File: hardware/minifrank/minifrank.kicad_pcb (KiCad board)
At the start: 4 copper layers, 85.6 x 54 mm, 136 parts, among them J1 PWR, J10 VGA, J11 PJ-320D, J12 104031-0811, J2 UART, J3 DEBUG, J4 SS-52100-004, J5 USB4215-03-A, J6 MDC-036, J7 PJ-320D, J8 DC3RX19JA2, J9 GP2, U1 TS3USB221RSER, U10 ESP-01v090, U11 TDA1387T, U12 LM358, U2 USBLC6-2SC6, U3 MW7211A, U4 AMS1117-3.3, U5 TXS0104ERGYR, U6 ESP-PSRAM32, U7 W25Q128JVS, U8 CD4069UBM, U9 RP2350, Y1 ASE-12MHz

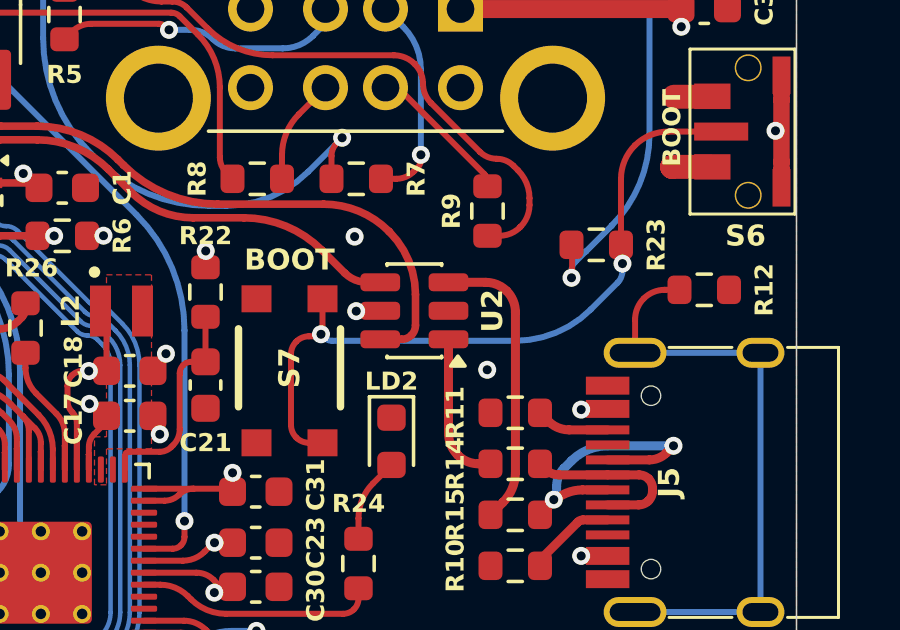
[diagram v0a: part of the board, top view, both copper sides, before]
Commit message: MiniFRANK: localize libs, recolor connectors, split audio jacks
- Split J7 (TapeIn) and J11 (AudioOut) into per-instance footprints
  and 3D models with light red and green plastic
- Unify connector metal shells to neutral 0.65 gray (USB, USB-C, SD,
  PS/2, switches, DB9, VGA, HDMI)
- Color VGA plastic body blue
- Replace HDMI IGES with project-local STEP and align footprint
- Move all 3D models and footprints to project-local 3d/ and libs/
- Merge cached schematic symbols into FRANK.kicad_sym; rewrite all
  schematic instances to use FRANK: lib_id; trim sym-lib-table
- Run kicad-cli sym/sch upgrade so cached symbols match library
- Remove unused footprints, symbols, and 3D files
- Regenerate minifrank-iso.png
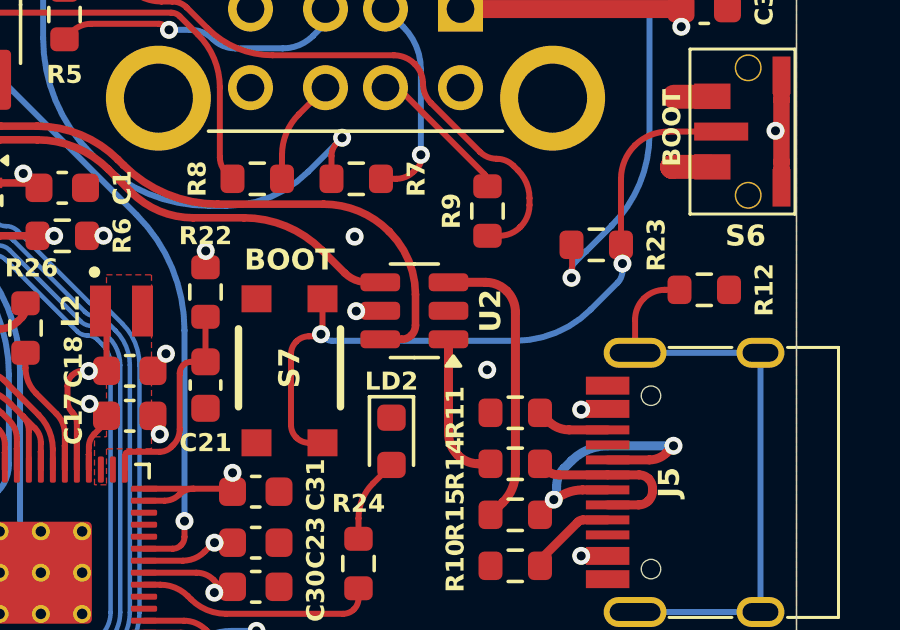
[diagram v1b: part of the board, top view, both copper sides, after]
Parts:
- J11: footprint FRANK:Jack (3.5mm, PJ-320D) -> FRANK:Jack (3.5mm, PJ-320D, AudioOut)
- J7: footprint FRANK:Jack (3.5mm, PJ-320D) -> FRANK:Jack (3.5mm, PJ-320D, TapeIn)
- U2: footprint Package_TO_SOT_SMD:SOT-23-6 -> FRANK:SOT-23-6

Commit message: fix: correct PSRAM part to ESP-PSRAM64H and clean up doc inaccuracies
Hardware:
- Rename ESP-PSRAM32 to ESP-PSRAM64H across MicroFRANK and MiniFRANK
  symbol libraries, schematics, PCB value fields and the SO-8 footprint
  default. Update datasheet URL to Espressif's combined ESP-PSRAM64 /
  ESP-PSRAM64H sheet.

Docs:
- Replace "SD card with firmware" wording everywhere with the correct
  "SD card with ROMs / disk images" plus an explicit BOOTSEL -> .uf2
  flashing step. RP2040 and RP2350 are not flashable from SD; the SD
  card holds runtime content read by the firmware.
- MicroFRANK: drop bogus TXS0104ERGYR from BOM and soldering steps;
  the part is not on this board (no PS/2, no gamepad, no 5 V signals).
- FRANK PGA: split the misleading "1 vs 2 audio multiplexer" comparison
  into separate audio-mux and USB-host-mux rows; FRANK PGA uses two
  74HC4052D, one for audio routing and one as the USB D+/D- multiplexer.
  Remove the stale TS3USB221 mention from the soldering steps.
- README and all four board guides (EN + RU): PSRAM type now reads
  ESP-PSRAM64H consistently.
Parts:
- U6: value ESP-PSRAM32 -> ESP-PSRAM64H
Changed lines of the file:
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@@
 			)
 		)
-		(property "Value" "ESP-PSRAM32"
+		(property "Value" "ESP-PSRAM64H"
 			(at 0 3.4 0)
 			(layer "F.Fab")
@@
 			)
 		)
-		(property "Datasheet" "https://www.espressif.com/sites/default/files/documentation/esp-psram32_datasheet_en.pdf"
+		(property "Datasheet" "https://www.espressif.com/sites/default/files/documentation/esp-psram64_esp-psram64h_datasheet_en.pdf"
 			(at 0 0 0)
 			(layer "F.Fab")

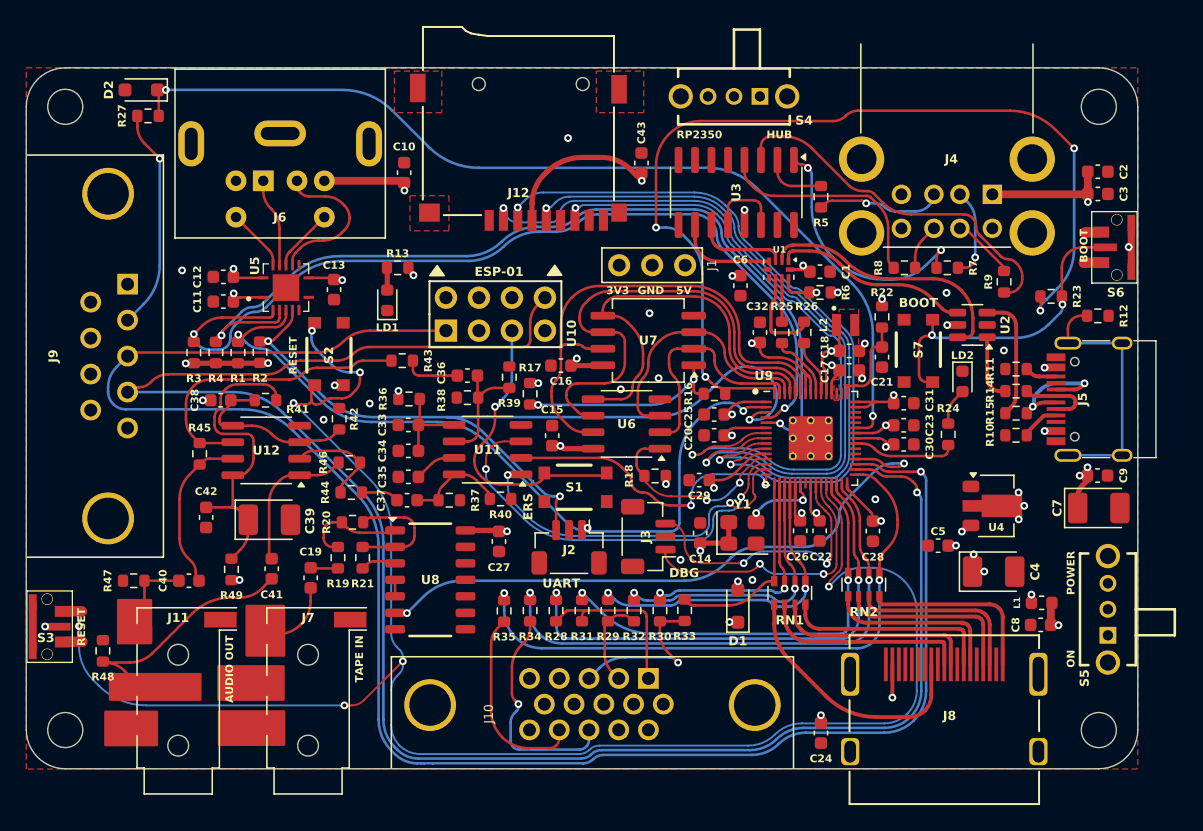
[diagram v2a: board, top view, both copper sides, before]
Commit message: docs: standardize naming (assembly.pdf, bom.html, schematics.pdf)
Latest versions:
- frank: 2.09
- frank_pga: 1.03
- microfrank: 1.02
- minifrank: 1.07
- nyx: 2.03
- xt8086: 1.04
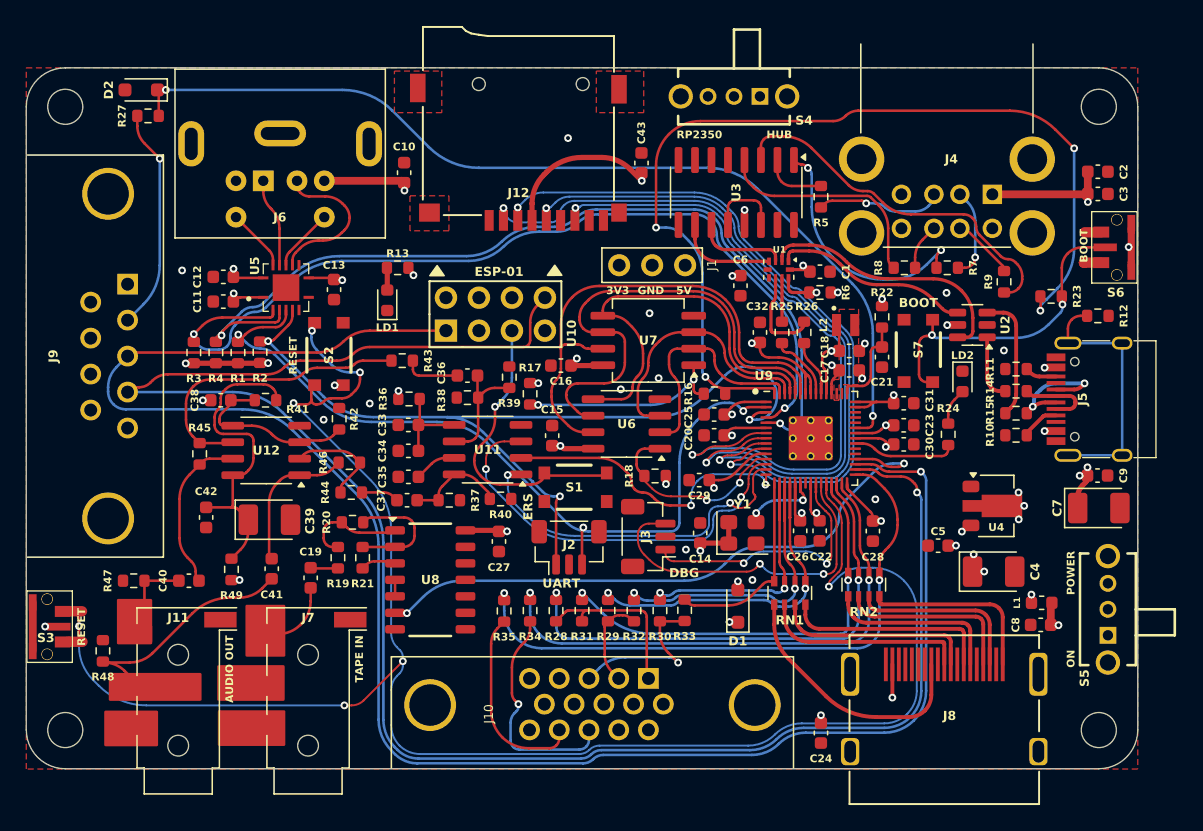
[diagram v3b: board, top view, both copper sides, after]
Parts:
- turned J2 to 0 degrees
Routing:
- net /RP2350A/SWD: track 21.7 -> 26.9 mm
- net /GPIO0: track 59.2 -> 62.1 mm
- net /GPIO1: track 65.9 -> 68.5 mm
- net /RP2350A/SWCLK: track 22.0 -> 21.2 mm

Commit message: MiniFRANK: new board version
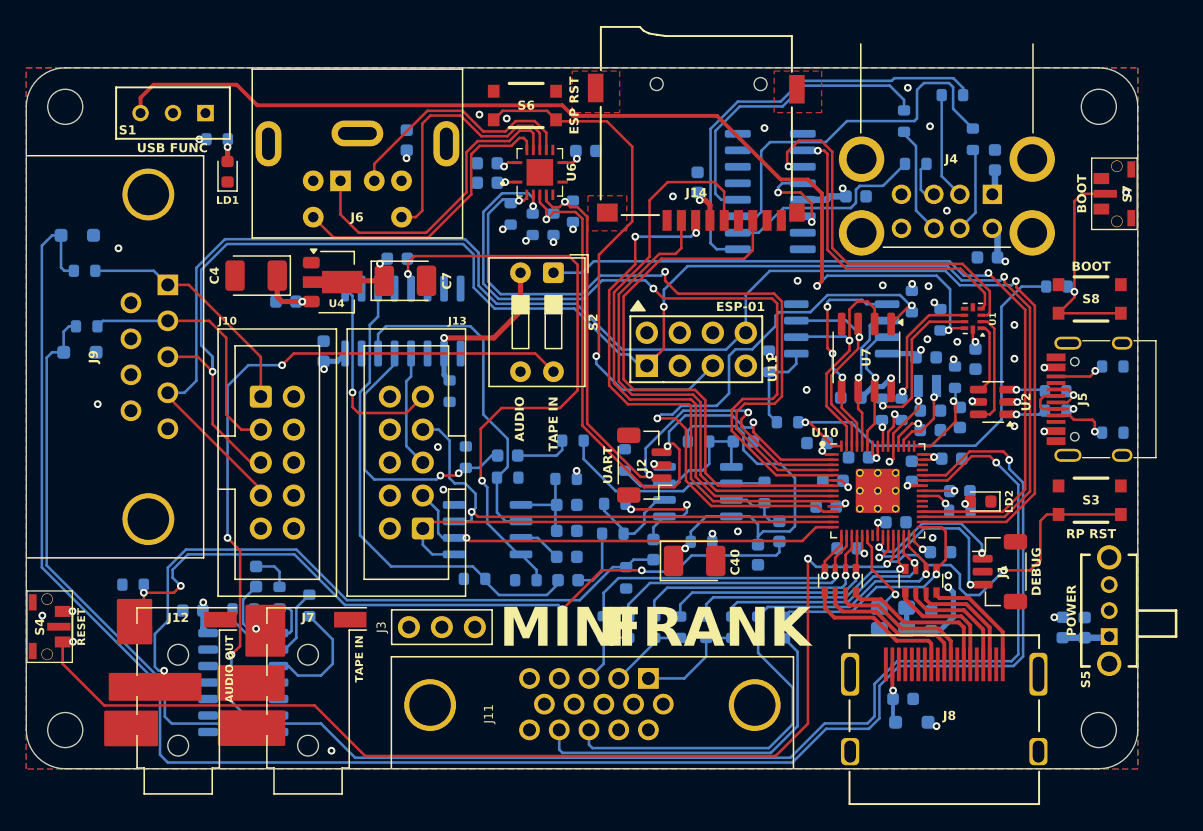
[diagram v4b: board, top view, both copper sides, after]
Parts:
- removed the R12 at (213.2, 82.9)
- removed the S4 at (187.2, 66.0)
- added C10: 100n, FRANK:C_0603_1608Metric, B.Cu at (153.6, 85.6)
- added D2: 3V3, FRANK:D_SOD-323, B.Cu at (134.6, 76.7)
- added J10: Conn_02x05_Top_Bottom, FRANK:IDC-Header_2x05_P2.54mm_Vertical, F.Cu at (148.8, 89.1)
- added J13: Ext_Sound, FRANK:IDC-Header_2x05_P2.54mm_Vertical, F.Cu at (161.2, 99.3)
- added R15: 10K, FRANK:R_0603_1608Metric, B.Cu at (163.3, 88.7)
- added R27: 1K, FRANK:R_0603_1608Metric, B.Cu at (135.2, 79.4)
- added S1: SS12D00, FRANK:Switch_Slide_SS12D00, F.Cu at (144.5, 67.3)
- added S2: SW_DIP_x02, FRANK:SW_DIP_SPSTx02_Slide_9.78x7.26mm_W7.62mm_P2.54mm, F.Cu at (171.3, 79.6)
- added U5: 74HC4052D, FRANK:SOP-16_P1.27mm, B.Cu at (159.7, 83.3)
- C1, C2, C3, C5, C6, C8, C9, L1, L2, R10, R11, R16, R17, R18, R19, R20, R21, R22, R23, R24, R25, R26, R5, R6, R7, R8, R9, U3, Y1: moved to B.Cu
- C11: renamed from C10; moved to B.Cu
- C12: renamed from C11; moved to B.Cu
- C13: renamed from C12; moved to B.Cu
- C14: renamed from C13; moved to B.Cu
- C15: renamed from C14; moved to B.Cu
- C16: renamed from C15; moved to B.Cu
- C17: renamed from C16; moved to B.Cu
- C18: renamed from C17; moved to B.Cu
- C19: renamed from C18; moved to B.Cu
- C20: renamed from C19; moved to B.Cu
- C21: renamed from C20; moved to B.Cu
- C22: renamed from C21; moved to B.Cu
- C23: renamed from C22; moved to B.Cu
- C24: renamed from C23; moved to B.Cu
- C25: renamed from C24; moved to B.Cu
- C26: renamed from C25; moved to B.Cu
- C27: renamed from C26; moved to B.Cu
- C28: renamed from C27; moved to B.Cu
- C29: renamed from C28; moved to B.Cu
- C30: renamed from C29; moved to B.Cu
- C31: renamed from C30; moved to B.Cu
- C32: renamed from C31; moved to B.Cu
- C33: renamed from C32; moved to B.Cu
- C34: renamed from C33; moved to B.Cu
- C35: renamed from C34; moved to B.Cu
- C36: renamed from C35; moved to B.Cu
- C37: renamed from C36; moved to B.Cu
- C38: renamed from C37; moved to B.Cu
- C39: renamed from C38; moved to B.Cu
- C4, C7: footprint FRANK:Capacitor (3528, tantalum, polar) -> FRANK:CP_EIA-3528-12_Kemet-T
- C40: renamed from C39; footprint FRANK:Capacitor (3528, tantalum, polar) -> FRANK:CP_EIA-3528-12_Kemet-T
- C41: renamed from C40; moved to B.Cu
- C42: renamed from C41; moved to B.Cu
- C43: renamed from C42; moved to B.Cu
- C44: renamed from C43; moved to B.Cu
- D1: footprint FRANK:Diode (SOD-323) -> FRANK:D_SOD-323; moved to B.Cu
- D3: renamed from D2; footprint FRANK:Diode (SOD-323) -> FRANK:D_SOD-323; moved to B.Cu
- H1, H2, H3, H4: footprint FRANK:Mounting Hole (2.7mm) -> FRANK:MountingHole_2.7mm
- J11: renamed from J10; footprint FRANK:D-SUB (15 pin, female) -> FRANK:DSUB-15_Female
- J12: renamed from J11; footprint FRANK:Jack (3.5mm, PJ-320D, AudioOut) -> FRANK:AudioJack_3.5mm_PJ320D_AudioOut
- J14: renamed from J12; footprint FRANK:MicroSD (SMD, long) -> FRANK:MicroSD_SMD_Long
- J3: renamed from J1; footprint FRANK:Pin Header (1x03) -> FRANK:PinHeader_1x03_P2.54mm
- J4: footprint FRANK:USB Type A (stacked) -> FRANK:USB_A_Stacked
- J5: footprint FRANK:USB Type C -> FRANK:USB_C_Receptacle
- J6: footprint FRANK:MiniDIN (6 Pin, female) -> FRANK:MiniDIN_6pin_Female
- J7: footprint FRANK:Jack (3.5mm, PJ-320D, TapeIn) -> FRANK:AudioJack_3.5mm_PJ320D_TapeIn
- J8: footprint FRANK:HDMI (female) -> FRANK:HDMI_Female
- J9: footprint FRANK:D-SUB (9 pin, male, top mount) -> FRANK:DSUB-9_Male_TopMount
- R1: renamed from R3; moved to B.Cu
- R12: renamed from R13; moved to B.Cu
- R13: renamed from R14; moved to B.Cu
- R14: renamed from R15; moved to B.Cu
- R2: renamed from R4; moved to B.Cu
- R28: renamed from R27; moved to B.Cu
- R29: renamed from R28; moved to B.Cu
- R3: renamed from R1; moved to B.Cu
- R30: renamed from R29; moved to B.Cu
- R31: renamed from R30; moved to B.Cu
- R32: renamed from R31; moved to B.Cu
- R33: renamed from R32; moved to B.Cu
- R34: renamed from R33; moved to B.Cu
- R35: renamed from R34; moved to B.Cu
- R36: renamed from R35; moved to B.Cu
- R37: renamed from R36; moved to B.Cu
- R38: renamed from R37; moved to B.Cu
- R39: renamed from R38; moved to B.Cu
- R4: renamed from R2; moved to B.Cu
- R40: renamed from R39; moved to B.Cu
- R41: renamed from R40; moved to B.Cu
- R42: renamed from R41; moved to B.Cu
- R43: renamed from R42; moved to B.Cu
- R44: renamed from R43; moved to B.Cu
- R45: renamed from R44; moved to B.Cu
- R46: renamed from R45; moved to B.Cu
- R47: renamed from R46; moved to B.Cu
- R48: renamed from R47; moved to B.Cu
- R49: renamed from R48; moved to B.Cu
- R50: renamed from R49; moved to B.Cu
- RN1, RN2: footprint FRANK:Resistor Array (4x0603) -> FRANK:R_Array_4x0603
- U10: renamed from U9; footprint FRANK:QFN 60 (RP2350A) -> FRANK:QFN-60_RP2350A
- U12: renamed from U11; moved to B.Cu
- U13: renamed from U12; moved to B.Cu
- U8: renamed from U7; moved to B.Cu
- U9: renamed from U8; moved to B.Cu
- moved C4 61.2 mm to (148.4, 79.8), turned to 180 degrees
- moved S3 59.7 mm to (212.7, 97.1), turned to 180 degrees
- moved C9 56.5 mm to (159.3, 78.5)
- moved C7 56.2 mm to (159.9, 80.2)
- moved U4 53.6 mm to (154.6, 80.3)
- moved C5 53.6 mm to (150.7, 81.8)
- moved C41 45.6 mm to (188.7, 99.5), turned to -90 degrees
- moved R46 43.6 mm to (187.6, 96.5)
- moved C43 42.6 mm to (187.1, 101.3)
- moved R49 40.7 mm to (176.9, 103.1), turned to 90 degrees
- moved C39 40.4 mm to (185.9, 92.6), turned to 180 degrees
- moved R50 36.3 mm to (182.7, 100.3), turned to 180 degrees
- moved R42 33.5 mm to (182.5, 92.6), turned to 180 degrees
- moved U13 33.4 mm to (182.4, 96.4), turned to 0 degrees
- moved C40 32.9 mm to (182.2, 101.8)
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- renumbered J3 to J1, S2 to S3, S3 to S4, S1 to S6, S6 to S7, S7 to S8, U10 to U11, U5 to U6, U6 to U7
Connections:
- net Net-(J9-Pad2) renamed /Gamepad/G_DATA1
- C37 pad 1: /Audio/TDA_L -> /Audio Multiplexer/AMP_IN_L
- C38 pad 1: /Audio/TDA_R -> /Audio Multiplexer/AMP_IN_R
- J14 pad 9: (no net) -> unconnected-(J14-DAT1-Pad9)
- J5 pad 13: Net-(J5-SHIELD) -> GND
- J9 pad 1: unconnected-(J9-Pad1) -> /Gamepad/G_DATA2
- R38 pad 1: /Audio/TDA_R -> /Audio Multiplexer/TDA_R
- R39 pad 2: /Audio/TDA_L -> /Audio Multiplexer/TDA_L
- R40 pad 1: /Audio/TDA_L -> /Audio Multiplexer/AMP_IN_L
- R41 pad 1: /Audio/TDA_R -> /Audio Multiplexer/AMP_IN_R
- U10 pad 41: /RP2350A/GPIO27 -> /GPIO27
- U12 pad 6: /Audio/TDA_L -> /Audio Multiplexer/TDA_L
- U12 pad 8: /Audio/TDA_R -> /Audio Multiplexer/TDA_R
- U9 pad 6: /GPIO22 -> /Tape In/LOAD_IN
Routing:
- net /GPIO27: track 0.00 -> 143.3 mm, vias 0 -> 1
- net /USBSW: track 21.1 -> 80.3 mm, vias 1 -> 2
- net /GPIO26: track 72.9 -> 129.5 mm, vias 2 -> 1
- net /Tape In/LOAD_IN: track 0.00 -> 56.0 mm, vias 0 -> 3
- net /Audio/AMP_OUTL: track 6.75 -> 58.8 mm, vias 0 -> 4
- net /Audio Multiplexer/TDA_R: track 0.00 -> 46.1 mm, vias 0 -> 2
- net /RP2350A/QSPI_SS: track 73.9 -> 33.0 mm, vias 4 -> 1
- net VBUS: track 199.8 -> 239.7 mm, vias 14 -> 11
- net /Audio Multiplexer/AMP_IN_R: track 0.00 -> 37.0 mm
- net /RUN: track 145.9 -> 111.5 mm, vias 7 -> 5
- net /RP2350A/GPIO8: track 15.0 -> 47.1 mm
- net /Audio/AMP_OUTR: track 18.1 -> 49.8 mm, vias 0 -> 1
- net /RP2350A/QSPI_SD3: track 39.7 -> 8.31 mm, vias 0 -> 1
- net +3V3: track 70.1 -> 40.1 mm, vias 28 -> 26
- net /GPIO19: track 46.1 -> 18.2 mm, vias 2 -> 1
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- added copper zone on B.Cu, net GND
- removed copper zone on F.Cu, net /RP2350A/VREG_LX
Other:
- board text added: "AUDIO"
- board text added: "DEBUG"
- board text added: "ESP RST"
- board text added: "RP RST"
- board text added: "USB FUNC"
- board text added: "© 2026 Mikhail Matveev HW ${VERSION} | ${DATE} https://frank.rh1.tech"
- board text removed: "3V3"
- board text removed: "5V"
- board text removed: "DBG"
- board text removed: "Designed by Mikhail Matveev HW ${VERSION} | ${DATE} https://frank.rh1.tech"
- board text removed: "ERS"
- board text removed: "GND"
- board text removed: "HUB"
- board text removed: "M2"
- board text removed: "ON"
- board text removed: "RP2350"
